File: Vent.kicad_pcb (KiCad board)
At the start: 4 copper layers, 38.1 x 17.6 mm, 26 parts, among them J2 B2B-XH-A_LF__SN_, J3 Conn_01x03_Pin, J4 Conn_01x04_Socket, SW1 SW_Push, U1 ESP32-H2-MINI-1-H2, U4 MCP1640x-xMC

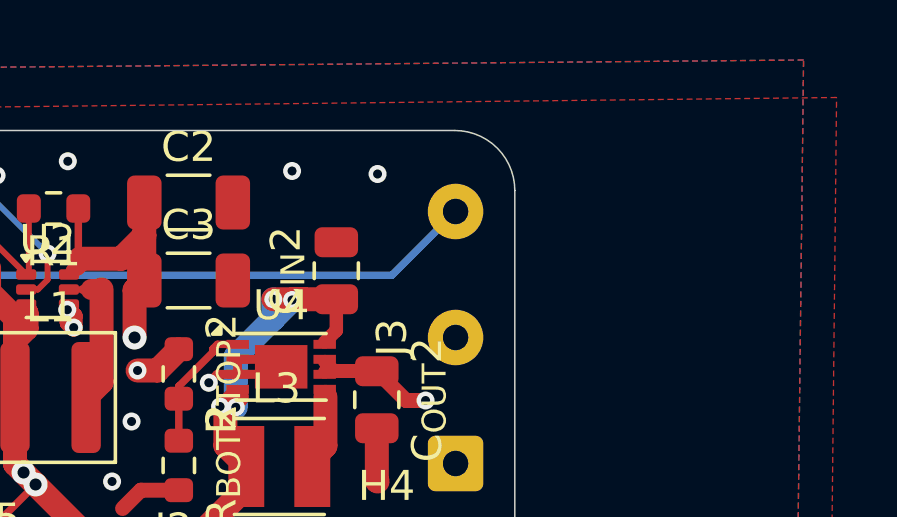
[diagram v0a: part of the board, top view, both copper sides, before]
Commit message: feat: Add project revision to PCB silkscreen
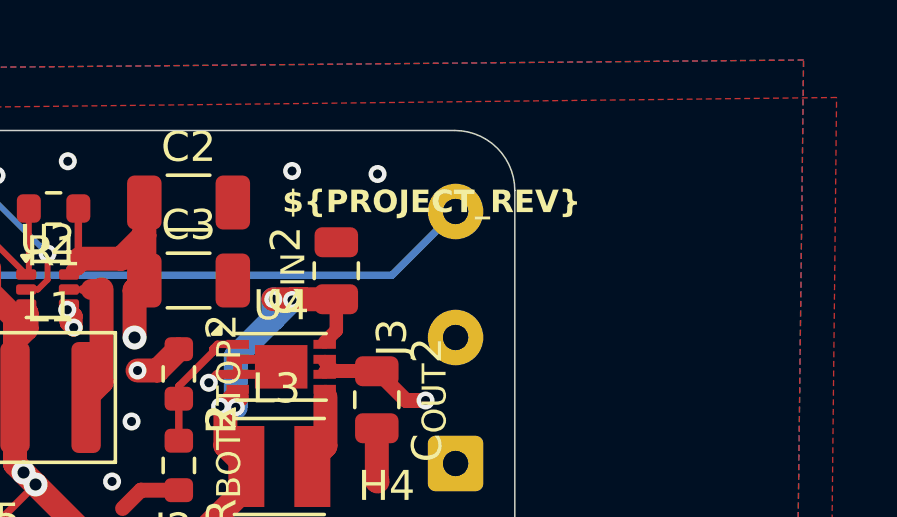
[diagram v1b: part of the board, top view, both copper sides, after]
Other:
- board text added: "${PROJECT_REV}"
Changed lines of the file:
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@@
 		)
 	)
+	(property "PROJECT_REV" "v0.1.0")
 	(footprint "MountingHole:MountingHole_2.2mm_M2"
 		(layer "F.Cu")
@@
 		(layer "Edge.Cuts")
 	)
+	(gr_text "${PROJECT_REV}"
+		(at 152.527 62.611 0)
+		(layer "F.SilkS")
+		(effects
+			(font
+				(size 0.75 0.75)
+				(bold yes)
+			)
+			(justify left bottom)
+		)
+	)
 	(segment

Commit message: feat: Fix most DRC rule violations
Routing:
- net GND: track 63.4 -> 62.9 mm, vias 33 -> 32
- net /BAT+: vias 6 -> 3
- net +3.3V: vias 5 -> 4
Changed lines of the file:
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@@
 		(capping no)
 		(filling no)
+		(zone_defaults)
 		(pcbplotparams
 			(layerselection 0x00000000_00000000_55555555_5755f5ff)
@@
 			(at 0 -3.15 0)
 			(layer "F.SilkS")
+			(hide yes)
 			(effects
 				(font
@@
 			(at 0 3.15 0)
 			(layer "F.Fab")
+			(hide yes)
 			(effects
 				(font
@@
 			(at 0 -1.43 90)
 			(layer "F.SilkS")
+			(hide yes)
 			(effects
 				(font
@@
 			(at 0 1.43 90)
 			(layer "F.Fab")
+			(hide yes)
 			(effects
 				(font
@@
 			(at 4.2 -2.12 90)
 			(layer "F.SilkS")
+			(hide yes)
 			(effects
 				(font
@@
 			(at 4.2 2.12 90)
 			(layer "F.Fab")
+			(hide yes)
 			(effects
 				(font
@@
 			(at 1.27 -1.96 0)
 			(layer "F.SilkS")
+			(hide yes)
 			(effects
 				(font
@@
 			(at 1.27 7.63 0)
 			(layer "F.Fab")
+			(hide yes)
 			(effects
 				(font
@@
 			(at 0 -1.05 90)
 			(layer "F.SilkS")
+			(hide yes)
 			(effects
 				(font
@@
 			(at 0 1.05 90)
 			(layer "F.Fab")
+			(hide yes)
 			(effects
 				(font
@@
 			(at 0 -3.15 0)
 			(layer "F.SilkS")
+			(hide yes)
 			(effects
 				(font
@@
 			(at 0 3.15 0)
 			(layer "F.Fab")
+			(hide yes)
 			(effects
 				(font
@@
 			(at 0 -1.05 0)
 			(layer "F.SilkS")
+			(hide yes)
 			(effects
 				(font
@@
 			(at 0 1.05 0)
 			(layer "F.Fab")
+			(hide yes)
 			(effects
 				(font
@@
 			(at 0 -1.05 90)
 			(layer "F.SilkS")
+			(hide yes)
 			(effects
 				(font
@@
 			(at 0 1.05 90)
 			(layer "F.Fab")
+			(hide yes)
 			(effects
 				(font
@@
 			(at 0 -1.85 0)
 			(layer "F.SilkS")
+			(hide yes)
 			(effects
 				(font
@@
 			(at 0 1.85 0)
 			(layer "F.Fab")
+			(hide yes)
 			(effects
 				(font
@@
 			(at 0 -1.85 0)
 			(layer "F.SilkS")
+			(hide yes)
 			(effects
 				(font
@@
 			(at 0 1.85 0)
 			(layer "F.Fab")
+			(hide yes)
 			(effects
 				(font
@@
 			(at 0 -1.43 180)
 			(layer "F.SilkS")
+			(hide yes)
 			(effects
 				(font
@@
 			(at 0 1.43 180)
 			(layer "F.Fab")
+			(hide yes)
 			(effects
 				(font
@@
 			(at 0 -1.68 90)
 			(layer "F.SilkS")
+			(hide yes)
 			(effects
 				(font
@@
 			(at 0 1.68 90)
 			(layer "F.Fab")
+			(hide yes)
 			(effects
 				(font
@@
 			(unlocked yes)
 			(layer "F.SilkS")
+			(hide yes)
 			(effects
 				(font
@@
 			(unlocked yes)
 			(layer "F.Fab")
+			(hide yes)
 			(effects
 				(font
@@
 			(at 0 -2.05 0)
 			(layer "F.SilkS")
+			(hide yes)
 			(effects
 				(font
@@
 			(at 0 2.05 0)
 			(layer "F.Fab")
+			(hide yes)
 			(effects
 				(font
@@
 			(at 0 -1.85 0)
 			(layer "F.SilkS")
+			(hide yes)
 			(effects
 				(font
@@
 			(at 0 1.85 0)
 			(layer "F.Fab")
+			(hide yes)
 			(effects
 				(font
@@
 			(at 0 -1.05 90)
 			(layer "F.SilkS")
+			(hide yes)
 			(effects
 				(font
@@
 			(at 0 1.05 90)
 			(layer "F.Fab")
+			(hide yes)
 			(effects
 				(font
@@
 			(at 0 -3 0)
 			(layer "F.SilkS")
+			(hide yes)
 			(effects
 				(font
@@
 			(at 0 3 0)
 			(layer "F.Fab")
+			(hide yes)
 			(effects
 				(font
@@
 			(at 0 2.7 0)
 			(layer "F.SilkS")
+			(hide yes)
 			(effects
 				(font
@@
 			(at 0 -2.3 0)
 			(layer "F.Fab")
+			(hide yes)
 			(effects
 				(font
@@
 			(at 0 -1.43 0)
 			(layer "F.SilkS")
+			(hide yes)
 			(effects
 				(font
@@
 			(at 0 1.43 0)
 			(layer "F.Fab")
+			(hide yes)
 			(effects
 				(font
@@
 			(at 0 -1.65 0)
 			(layer "F.SilkS")
+			(hide yes)
 			(effects
 				(font
@@
 			(at 0 1.65 0)
 			(layer "F.Fab")
+			(hide yes)
 			(effects
 				(font
@@
 			(at 0 -1.43 90)
 			(layer "F.SilkS")
+			(hide yes)
 			(effects
 				(font
@@
 			(at 0 1.43 90)
 			(layer "F.Fab")
+			(hide yes)
 			(effects
 				(font
@@
 			(at 0 -9.5 0)
 			(layer "F.SilkS")
+			(hide yes)
 			(effects
 				(font
@@
 			(at 0 9.85 0)
 			(layer "F.Fab")
+			(hide yes)
 			(effects
 				(font
@@
 			(at 0 -1.68 90)
 			(layer "F.SilkS")
+			(hide yes)
 			(effects
 				(font
@@
 			(at 0 1.68 90)
 			(layer "F.Fab")
+			(hide yes)
 			(effects
 				(font
@@
 			(at 0 -1.43 0)
 			(layer "F.SilkS")
+			(hide yes)
 			(effects
 				(font
@@
 			(at 0 1.43 0)
 			(layer "F.Fab")
+			(hide yes)
 			(effects
 				(font
@@
 			(at 2.3 -2.28 0)
 			(layer "F.SilkS")
+			(hide yes)
 			(effects
 				(font
@@
 			(at 2.3 2.28 0)
 			(layer "F.Fab")
+			(hide yes)
 			(effects
 				(font
@@
 			(at 0 2.6 90)
 			(layer "B.SilkS")
+			(hide yes)
 			(effects
 				(font
@@
 			(at 0 -2.6 90)
 			(layer "B.Fab")
+			(hide yes)
 			(effects
 				(font
@@
 	)
 	(segment
+		(start 141.7 73.057)
+		(end 141.732 73.025)
+		(width 0.35)
+		(layer "F.Cu")
+		(net "GND")
+	)
+	(segment
 		(start 145.403626 66.202114)
 		(end 145.403626 66.188336)
@@
 	)
 	(segment
-		(start 142.275 73.125)
-		(end 142.3 73.1)
-		(width 0.35)
-		(layer "F.Cu")
-		(net "GND")
-	)
-	(segment
 		(start 137.7 74.785298)
 		(end 138.226 74.259298)
@@
 	)
 	(segment
+		(start 141.7 73.125)
+		(end 141.7 73.057)
+		(width 0.35)
+		(layer "F.Cu")
+		(net "GND")
+	)
+	(segment
 		(start 145.57061 66.369098)
 		(end 145.57061 65.988383)
@@
 	)
 	(segment
-		(start 141.7 73.125)
-		(end 142.275 73.125)
-		(width 0.35)
-		(layer "F.Cu")
-		(net "GND")
-	)
-	(segment
 		(start 145.357227 65.708214)
 		(end 145.4125 65.652941)
@@
 	)
 	(via
-		(at 142.3 73.1)
-		(size 0.6)
-		(drill 0.3)
-		(layers "F.Cu" "B.Cu")
-		(free yes)
-		(net "GND")
-	)
-	(via
 		(at 145.375 60.825)
 		(size 0.6)
@@
 	)
 	(via
-		(at 150.45 69)
-		(size 0.6)
-		(drill 0.3)
-		(layers "F.Cu" "B.Cu")
-		(net "/BAT+")
-	)
-	(via
-		(at 144.3 71.6)
-		(size 0.8)
-		(drill 0.4)
-		(layers "F.Cu" "B.Cu")
-		(capping no)
-		(covering
-			(front no)
-			(back no)
-		)
-		(plugging
-			(front no)
-			(back no)
-		)
-		(filling no)
-		(net "/BAT+")
-	)
-	(via
 		(at 152.85 65.45)
 		(size 0.6)
@@
 		(net "/BAT+")
 	)
-	(via
-		(at 143.9 71.2)
-		(size 0.8)
-		(drill 0.4)
-		(layers "F.Cu" "B.Cu")
-		(capping no)
-		(covering
-			(front no)
-			(back no)
-		)
-		(plugging
-			(front no)
-			(back no)
-		)
-		(filling no)
-		(net "/BAT+")
-	)
 	(segment
 		(start 152.225 65.425)
@@
 	)
 	(via
-		(at 147.5 69.5)
-		(size 0.6)
-		(drill 0.3)
-		(layers "F.Cu" "B.Cu")
-		(net "+3.3V")
-	)
-	(via
 		(at 137.6 74)
 		(size 0.6)
@@
 	)
 	(zone
-		(net "GND")
-		(layer "F.Cu")
-		(hatch edge 0.5)
-		(connect_pads
-			(clearance 0.5)
-		)
-		(min_thickness 0.25)
-		(fill yes
-			(thermal_gap 0.5)
-			(thermal_bridge_width 0.5)
-			(island_removal_mode 0)
-		)
-		(polygon
-			(pts
-				(xy 117.6 59.3) (xy 117.7 77.8) (xy 170.8 77.6) (xy 171 58.7)
-			)
-		)
-	)
-	(zone
